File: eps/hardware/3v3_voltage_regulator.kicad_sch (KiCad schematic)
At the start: 16 parts, among them U39 MP28167-A

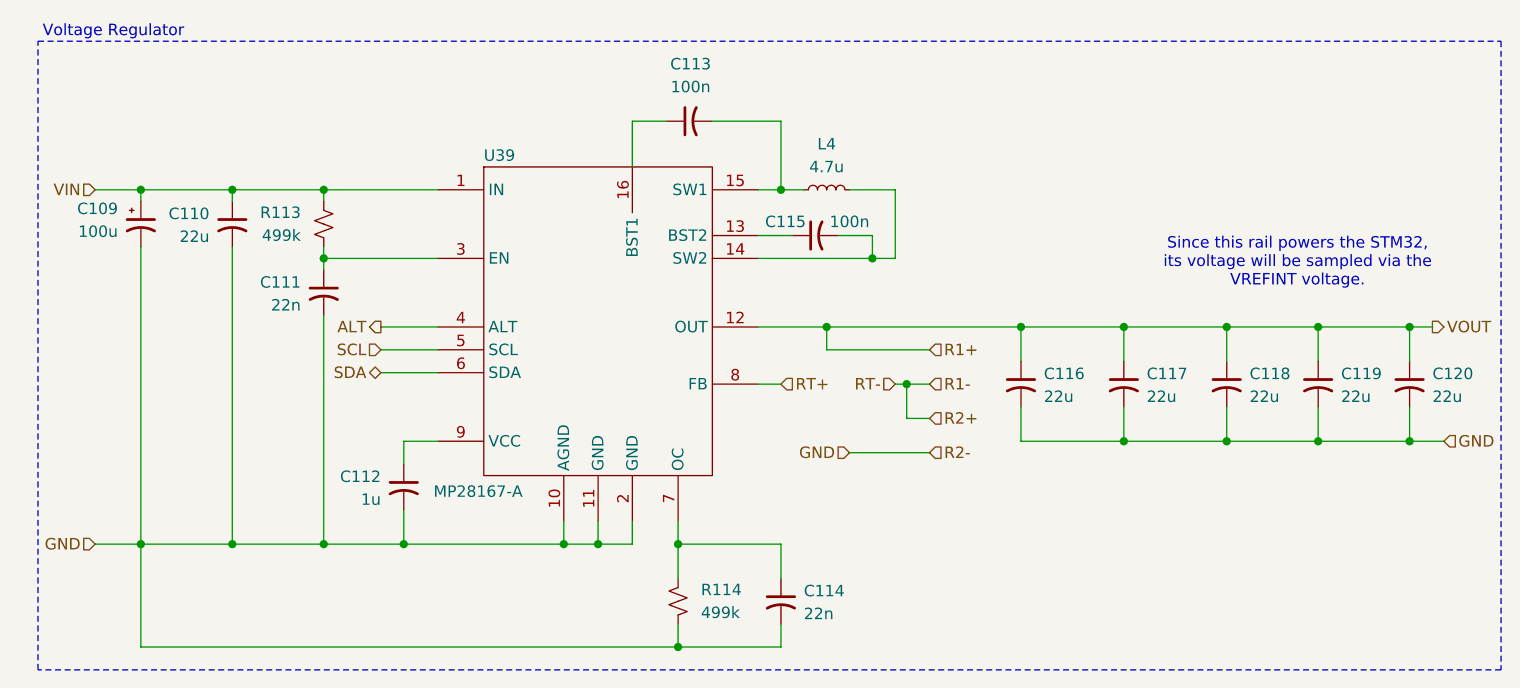
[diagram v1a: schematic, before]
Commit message: fix all ERC errors
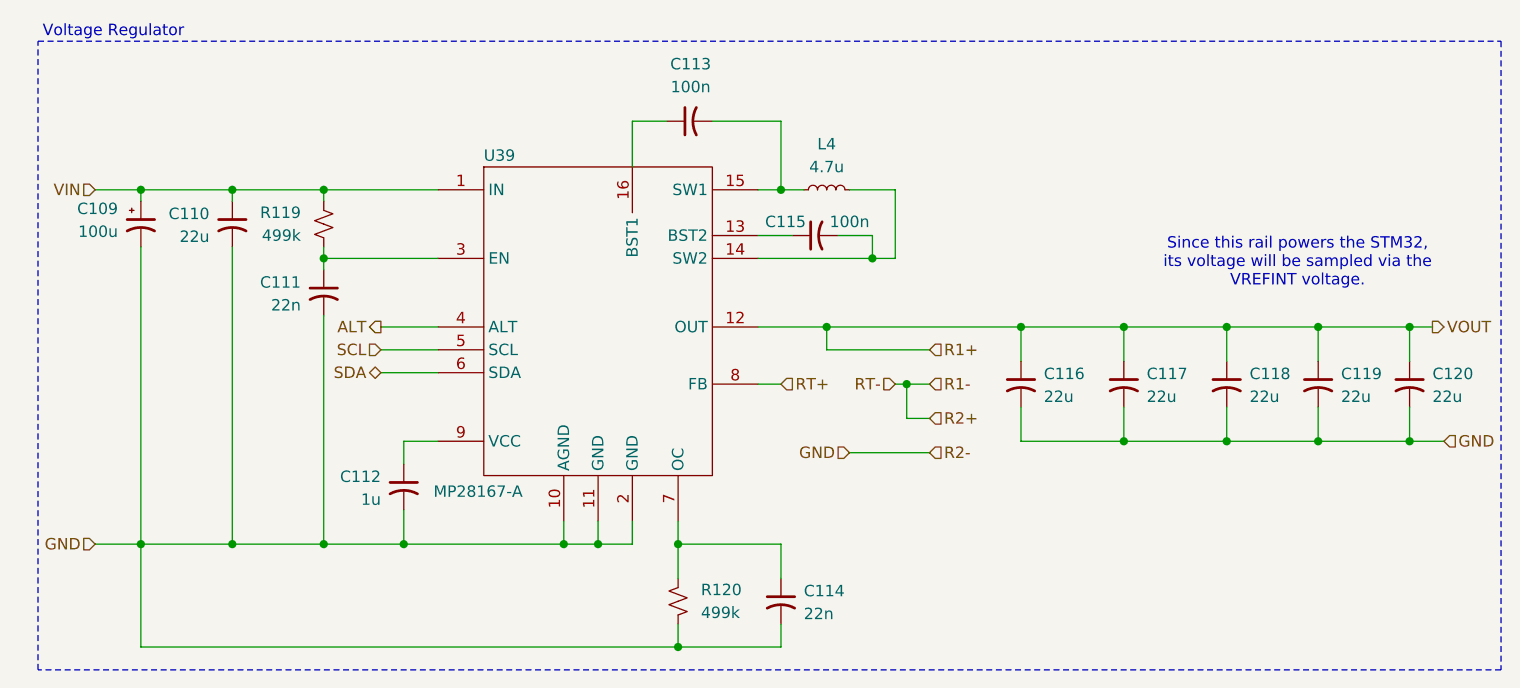
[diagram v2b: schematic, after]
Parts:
- renumbered R113 to R119, R114 to R120
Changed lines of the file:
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@@
 		(on_board yes)
 		(dnp no)
-		(property "Reference" "R113"
+		(property "Reference" "R119"
 			(at 107.95 78.7399 0)
 			(effects
@@
 			(project "eps"
 				(path "/9e0ae2e7-d4be-41b4-8312-0d2aceea2180/1a512821-4e0c-4fd8-8856-c70dc3f2d44d"
-					(reference "R113")
+					(reference "R119")
 					(unit 1)
 				)
@@
 		(on_board yes)
 		(dnp no)
-		(property "Reference" "R114"
+		(property "Reference" "R120"
 			(at 152.4 120.6499 0)
 			(effects
@@
 			(project "eps"
 				(path "/9e0ae2e7-d4be-41b4-8312-0d2aceea2180/1a512821-4e0c-4fd8-8856-c70dc3f2d44d"
-					(reference "R114")
+					(reference "R120")
 					(unit 1)
 				)

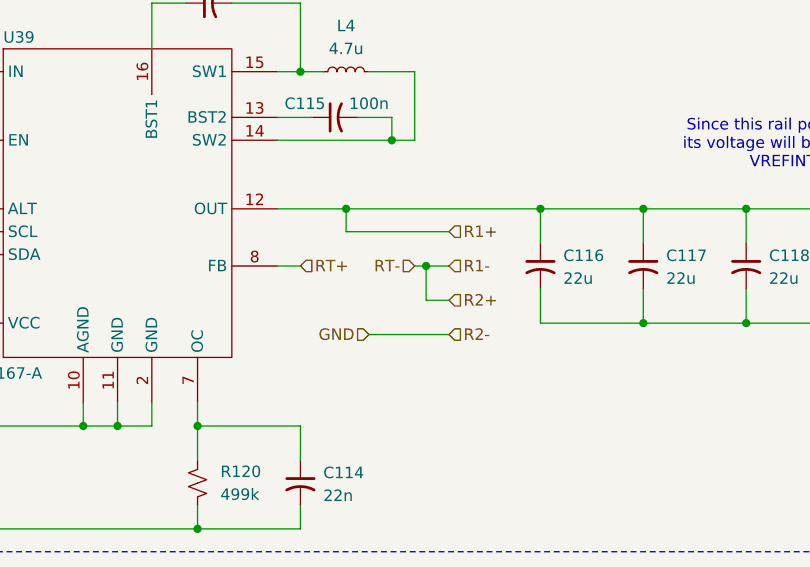
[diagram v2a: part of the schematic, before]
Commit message: fix all but one warning
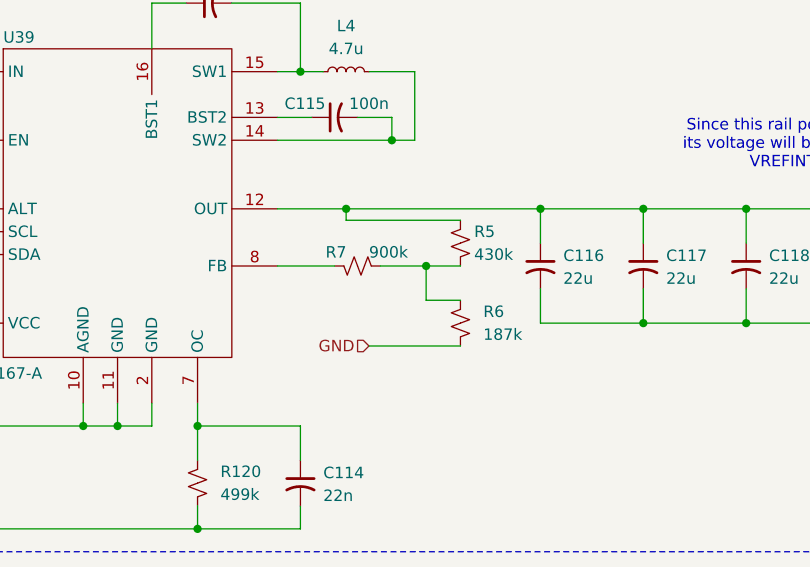
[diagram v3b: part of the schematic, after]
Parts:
- added R5: 430k, symbol Device:R_Small_US
- added R6: 187k, symbol Device:R_Small_US
- added R7: 900k, symbol Device:R_Small_US
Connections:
- net GND: now also R6.2
- net R1+ renamed VOUT
- net VOUT: now also R5.1
- net RT+: no longer names the net of U39.8 (FB)
- net RT+: now also R7.1
- new net: R5.2, R6.1, R7.2

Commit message: netlist fixes
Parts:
- renumbered R119 to R107, R120 to R108, R7 to R109, R5 to R110, R6 to R111
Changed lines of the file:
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@@
 		(on_board yes)
 		(dnp no)
-		(property "Reference" "R7"
-			(at 164.084 96.266 90)
+		(property "Reference" "R109"
+			(at 161.544 96.266 90)
 			(effects
 				(font
@@
 			(project "eps"
 				(path "/9e0ae2e7-d4be-41b4-8312-0d2aceea2180/1a512821-4e0c-4fd8-8856-c70dc3f2d44d"
-					(reference "R7")
+					(reference "R109")
 					(unit 1)
 				)
@@
 		(on_board yes)
 		(dnp no)
-		(property "Reference" "R5"
+		(property "Reference" "R110"
 			(at 180.594 93.98 0)
 			(effects
@@
 			(project "eps"
 				(path "/9e0ae2e7-d4be-41b4-8312-0d2aceea2180/1a512821-4e0c-4fd8-8856-c70dc3f2d44d"
-					(reference "R5")
+					(reference "R110")
 					(unit 1)
 				)
@@
 		(on_board yes)
 		(dnp no)
-		(property "Reference" "R6"
+		(property "Reference" "R111"
 			(at 181.61 102.8699 0)
 			(effects
@@
 			(project "eps"
 				(path "/9e0ae2e7-d4be-41b4-8312-0d2aceea2180/1a512821-4e0c-4fd8-8856-c70dc3f2d44d"
-					(reference "R6")
+					(reference "R111")
 					(unit 1)
 				)
@@
 		(on_board yes)
 		(dnp no)
-		(property "Reference" "R119"
+		(property "Reference" "R107"
 			(at 107.95 78.7399 0)
 			(effects
@@
 			(project "eps"
 				(path "/9e0ae2e7-d4be-41b4-8312-0d2aceea2180/1a512821-4e0c-4fd8-8856-c70dc3f2d44d"
-					(reference "R119")
+					(reference "R107")
 					(unit 1)
 				)
@@
 		(on_board yes)
 		(dnp no)
-		(property "Reference" "R120"
+		(property "Reference" "R108"
 			(at 152.4 120.6499 0)
 			(effects
@@
 			(project "eps"
 				(path "/9e0ae2e7-d4be-41b4-8312-0d2aceea2180/1a512821-4e0c-4fd8-8856-c70dc3f2d44d"
-					(reference "R120")
-					(unit 1)
-				)
+					(reference "R108")
+					(unit 1)
+				)

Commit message: start footprint assignment
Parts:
- C109: footprint (none) -> Capacitor_Tantalum_SMD:CP_EIA-3216-18_Kemet-A
- C110, C111, C112, C113, C114, C115, C116, C117, C118, C119, C120: footprint (none) -> Capacitor_SMD:C_0603_1608Metric
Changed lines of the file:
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@@
 			)
 		)
-		(property "Footprint" ""
+		(property "Footprint" "Capacitor_SMD:C_0603_1608Metric"
 			(at 220.98 97.79 0)
 			(effects
@@
 			)
 		)
-		(property "Footprint" ""
+		(property "Footprint" "Capacitor_SMD:C_0603_1608Metric"
 			(at 161.29 121.92 0)
 			(effects
@@
 			)
 		)
-		(property "Footprint" ""
+		(property "Footprint" "Capacitor_SMD:C_0603_1608Metric"
 			(at 119.38 109.22 0)
 			(effects
@@
 			)
 		)
-		(property "Footprint" ""
+		(property "Footprint" "Capacitor_SMD:C_0603_1608Metric"
 			(at 151.13 68.58 0)
 			(effects
@@
 			)
 		)
-		(property "Footprint" ""
+		(property "Footprint" "Capacitor_SMD:C_0603_1608Metric"
 			(at 231.14 97.79 0)
 			(effects
@@
 			)
 		)
-		(property "Footprint" ""
+		(property "Footprint" "Capacitor_SMD:C_0603_1608Metric"
 			(at 199.39 97.79 0)
 			(effects
@@
 			)
 		)
-		(property "Footprint" ""
+		(property "Footprint" "Capacitor_SMD:C_0603_1608Metric"
 			(at 187.96 97.79 0)
 			(effects
@@
 			)
 		)
-		(property "Footprint" ""
+		(property "Footprint" "Capacitor_SMD:C_0603_1608Metric"
 			(at 110.49 87.63 0)
 			(effects
@@
 			)
 		)
-		(property "Footprint" ""
+		(property "Footprint" "Capacitor_SMD:C_0603_1608Metric"
 			(at 100.33 80.01 0)
 			(effects
@@
 			)
 		)
-		(property "Footprint" ""
+		(property "Footprint" "Capacitor_SMD:C_0603_1608Metric"
 			(at 210.82 97.79 0)
 			(effects
@@
 			)
 		)
-		(property "Footprint" ""
+		(property "Footprint" "Capacitor_Tantalum_SMD:CP_EIA-3216-18_Kemet-A"
 			(at 90.17 80.01 0)
 			(effects
@@
 			)
 		)
-		(property "Footprint" ""
+		(property "Footprint" "Capacitor_SMD:C_0603_1608Metric"
 			(at 165.1 81.28 0)
 			(effects

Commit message: finish footprint assignment and board setup
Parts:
- L4: footprint (none) -> Inductor_SMD:L_Vishay_IHLP-2020
- R107, R108, R109, R110, R111: footprint (none) -> Resistor_SMD:R_0603_1608Metric
- U39: footprint (none) -> Package_DFN_QFN:MPS_QFN-16_3x3mm_P0.5mm
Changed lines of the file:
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@@
 			)
 		)
-		(property "Footprint" ""
+		(property "Footprint" "Package_DFN_QFN:MPS_QFN-16_3x3mm_P0.5mm"
 			(at 140.97 91.44 0)
 			(effects
@@
 			)
 		)
-		(property "Footprint" ""
+		(property "Footprint" "Resistor_SMD:R_0603_1608Metric"
 			(at 167.64 97.79 0)
 			(effects
@@
 			)
 		)
-		(property "Footprint" ""
+		(property "Footprint" "Inductor_SMD:L_Vishay_IHLP-2020"
 			(at 166.37 76.2 0)
 			(effects
@@
 			)
 		)
-		(property "Footprint" ""
+		(property "Footprint" "Resistor_SMD:R_0603_1608Metric"
 			(at 179.07 95.25 0)
 			(effects
@@
 			)
 		)
-		(property "Footprint" ""
+		(property "Footprint" "Resistor_SMD:R_0603_1608Metric"
 			(at 179.07 104.14 0)
 			(effects
@@
 			)
 		)
-		(property "Footprint" ""
+		(property "Footprint" "Resistor_SMD:R_0603_1608Metric"
 			(at 110.49 80.01 0)
 			(effects
@@
 			)
 		)
-		(property "Footprint" ""
+		(property "Footprint" "Resistor_SMD:R_0603_1608Metric"
 			(at 149.86 121.92 0)
 			(effects

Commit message: schematic fixes
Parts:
- C110, C111, C112, C113, C114, C115, C116, C117, C118, C119, C120: footprint Capacitor_SMD:C_0603_1608Metric -> Capacitor_SMD:C_0402_1005Metric
- R107, R108, R109, R110, R111: footprint Resistor_SMD:R_0603_1608Metric -> Resistor_SMD:R_0402_1005Metric
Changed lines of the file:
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@@
 			)
 		)
-		(property "Footprint" "Resistor_SMD:R_0603_1608Metric"
+		(property "Footprint" "Resistor_SMD:R_0402_1005Metric"
 			(at 167.64 97.79 0)
 			(effects
@@
 			)
 		)
-		(property "Footprint" "Capacitor_SMD:C_0603_1608Metric"
+		(property "Footprint" "Capacitor_SMD:C_0402_1005Metric"
 			(at 220.98 97.79 0)
 			(effects
@@
 			)
 		)
-		(property "Footprint" "Capacitor_SMD:C_0603_1608Metric"
+		(property "Footprint" "Capacitor_SMD:C_0402_1005Metric"
 			(at 161.29 121.92 0)
 			(effects
@@
 			)
 		)
-		(property "Footprint" "Capacitor_SMD:C_0603_1608Metric"
+		(property "Footprint" "Capacitor_SMD:C_0402_1005Metric"
 			(at 119.38 109.22 0)
 			(effects
@@
 			)
 		)
-		(property "Footprint" "Capacitor_SMD:C_0603_1608Metric"
+		(property "Footprint" "Capacitor_SMD:C_0402_1005Metric"
 			(at 151.13 68.58 0)
 			(effects
@@
 			)
 		)
-		(property "Footprint" "Capacitor_SMD:C_0603_1608Metric"
+		(property "Footprint" "Capacitor_SMD:C_0402_1005Metric"
 			(at 231.14 97.79 0)
 			(effects
@@
 			)
 		)
-		(property "Footprint" "Resistor_SMD:R_0603_1608Metric"
+		(property "Footprint" "Resistor_SMD:R_0402_1005Metric"
 			(at 179.07 95.25 0)
 			(effects
@@
 			)
 		)
-		(property "Footprint" "Capacitor_SMD:C_0603_1608Metric"
+		(property "Footprint" "Capacitor_SMD:C_0402_1005Metric"
 			(at 199.39 97.79 0)
 			(effects
@@
 			)
 		)
-		(property "Footprint" "Capacitor_SMD:C_0603_1608Metric"
+		(property "Footprint" "Capacitor_SMD:C_0402_1005Metric"
 			(at 187.96 97.79 0)
 			(effects
@@
 			)
 		)
-		(property "Footprint" "Capacitor_SMD:C_0603_1608Metric"
+		(property "Footprint" "Capacitor_SMD:C_0402_1005Metric"
 			(at 110.49 87.63 0)
 			(effects
@@
 			)
 		)
-		(property "Footprint" "Capacitor_SMD:C_0603_1608Metric"
+		(property "Footprint" "Capacitor_SMD:C_0402_1005Metric"
 			(at 100.33 80.01 0)
 			(effects
@@
 			)
 		)
-		(property "Footprint" "Resistor_SMD:R_0603_1608Metric"
+		(property "Footprint" "Resistor_SMD:R_0402_1005Metric"
 			(at 179.07 104.14 0)
 			(effects
@@
 			)
 		)
-		(property "Footprint" "Capacitor_SMD:C_0603_1608Metric"
+		(property "Footprint" "Capacitor_SMD:C_0402_1005Metric"
 			(at 210.82 97.79 0)
 			(effects
@@
 			)
 		)
-		(property "Footprint" "Resistor_SMD:R_0603_1608Metric"
+		(property "Footprint" "Resistor_SMD:R_0402_1005Metric"
 			(at 110.49 80.01 0)
 			(effects
@@
 			)
 		)
-		(property "Footprint" "Capacitor_SMD:C_0603_1608Metric"
+		(property "Footprint" "Capacitor_SMD:C_0402_1005Metric"
 			(at 165.1 81.28 0)
 			(effects
@@
 			)
 		)
-		(property "Footprint" "Resistor_SMD:R_0603_1608Metric"
+		(property "Footprint" "Resistor_SMD:R_0402_1005Metric"
 			(at 149.86 121.92 0)
 			(effects

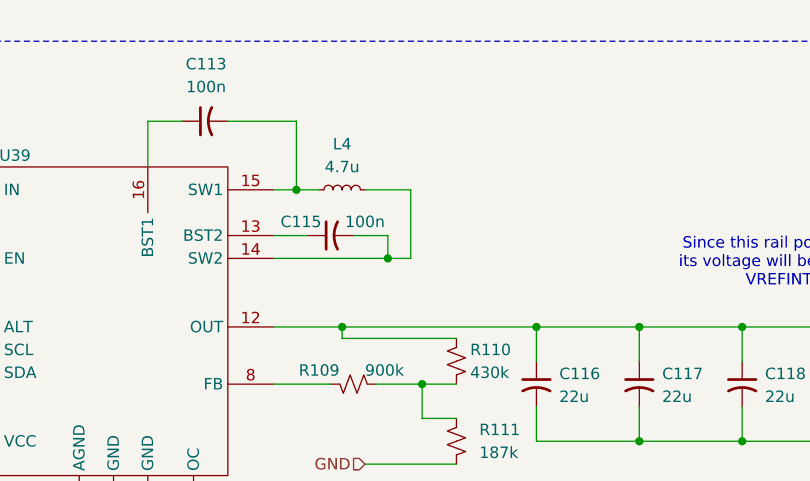
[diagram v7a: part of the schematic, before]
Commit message: fix placements and start routing voltage regulator
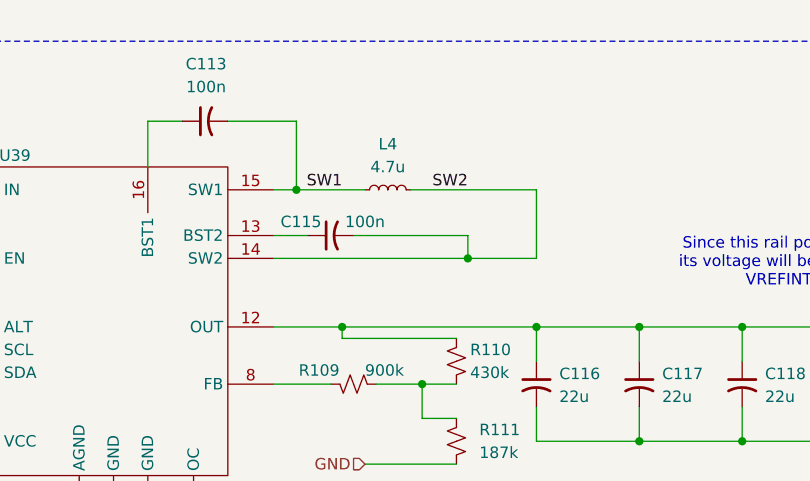
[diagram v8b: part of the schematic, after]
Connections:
- net SW2: now reaches C115.2, L4.2, U39.14 (SW2)
- net SW1: now reaches C113.2, L4.1, U39.15 (SW1)
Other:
- moved on the sheet: L4
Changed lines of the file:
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@@
-	)
-	(junction
-		(at 171.45 83.82)
-		(diameter 0)
-		(color 0 0 0 0)
 	)
 	(junction
@@
 	)
 	(junction
+		(at 137.16 115.57)
+		(diameter 0)
+		(color 0 0 0 0)
+	)
+	(junction
+		(at 210.82 91.44)
+		(diameter 0)
+		(color 0 0 0 0)
+	)
+	(junction
+		(at 149.86 115.57)
+		(diameter 0)
+		(color 0 0 0 0)
+	)
+	(junction
+		(at 166.37 91.44)
+		(diameter 0)
+		(color 0 0 0 0)
+	)
+	(junction
+		(at 119.38 115.57)
+		(diameter 0)
+		(color 0 0 0 0)
+	)
+	(junction
+		(at 231.14 91.44)
+		(diameter 0)
+		(color 0 0 0 0)
+	)
+	(junction
+		(at 110.49 83.82)
+		(diameter 0)
+		(color 0 0 0 0)
+	)
+	(junction
+		(at 140.97 115.57)
+		(diameter 0)
+		(color 0 0 0 0)
+	)
+	(junction
+		(at 110.49 76.2)
+		(diameter 0)
+		(color 0 0 0 0)
+	)
+	(junction
+		(at 220.98 91.44)
+		(diameter 0)
+		(color 0 0 0 0)
+	)
+	(junction
+		(at 187.96 91.44)
+		(diameter 0)
+		(color 0 0 0 0)
+	)
+	(junction
+		(at 90.17 115.57)
+		(diameter 0)
+		(color 0 0 0 0)
+	)
+	(junction
+		(at 210.82 104.14)
+		(diameter 0)
+		(color 0 0 0 0)
+	)
+	(junction
+		(at 90.17 76.2)
+		(diameter 0)
+		(color 0 0 0 0)
+	)
+	(junction
+		(at 175.26 97.79)
+		(diameter 0)
+		(color 0 0 0 0)
+	)
+	(junction
+		(at 199.39 104.14)
+		(diameter 0)
+		(color 0 0 0 0)
+	)
+	(junction
+		(at 110.49 115.57)
+		(diameter 0)
+		(color 0 0 0 0)
+	)
+	(junction
+		(at 100.33 115.57)
+		(diameter 0)
+		(color 0 0 0 0)
+	)
+	(junction
+		(at 180.34 83.82)
+		(diameter 0)
+		(color 0 0 0 0)
+	)
+	(junction
+		(at 231.14 104.14)
+		(diameter 0)
+		(color 0 0 0 0)
+	)
+	(junction
+		(at 100.33 76.2)
+		(diameter 0)
+		(color 0 0 0 0)
+	)
+	(junction
+		(at 220.98 104.14)
+		(diameter 0)
+		(color 0 0 0 0)
+	)
+	(junction
+		(at 199.39 91.44)
+		(diameter 0)
+		(color 0 0 0 0)
+	)
+	(junction
 		(at 161.29 76.2)
 		(diameter 0)
 		(color 0 0 0 0)
 	)
-	(junction
-		(at 137.16 115.57)
-		(diameter 0)
-		(color 0 0 0 0)
-	)
-	(junction
-		(at 210.82 91.44)
-		(diameter 0)
-		(color 0 0 0 0)
-	)
-	(junction
-		(at 149.86 115.57)
-		(diameter 0)
-		(color 0 0 0 0)
-	)
-	(junction
-		(at 166.37 91.44)
-		(diameter 0)
-		(color 0 0 0 0)
-	)
-	(junction
-		(at 119.38 115.57)
-		(diameter 0)
-		(color 0 0 0 0)
-	)
-	(junction
-		(at 231.14 91.44)
-		(diameter 0)
-		(color 0 0 0 0)
-	)
-	(junction
-		(at 110.49 83.82)
-		(diameter 0)
-		(color 0 0 0 0)
-	)
-	(junction
-		(at 140.97 115.57)
-		(diameter 0)
-		(color 0 0 0 0)
-	)
-	(junction
-		(at 110.49 76.2)
-		(diameter 0)
-		(color 0 0 0 0)
-	)
-	(junction
-		(at 220.98 91.44)
-		(diameter 0)
-		(color 0 0 0 0)
-	)
-	(junction
-		(at 187.96 91.44)
-		(diameter 0)
-		(color 0 0 0 0)
-	)
-	(junction
-		(at 90.17 115.57)
-		(diameter 0)
-		(color 0 0 0 0)
-	)
-	(junction
-		(at 210.82 104.14)
-		(diameter 0)
-		(color 0 0 0 0)
-	)
-	(junction
-		(at 90.17 76.2)
-		(diameter 0)
-		(color 0 0 0 0)
-	)
-	(junction
-		(at 175.26 97.79)
-		(diameter 0)
-		(color 0 0 0 0)
-	)
-	(junction
-		(at 199.39 104.14)
-		(diameter 0)
-		(color 0 0 0 0)
-	)
-	(junction
-		(at 110.49 115.57)
-		(diameter 0)
-		(color 0 0 0 0)
-	)
-	(junction
-		(at 100.33 115.57)
-		(diameter 0)
-		(color 0 0 0 0)
-	)
-	(junction
-		(at 231.14 104.14)
-		(diameter 0)
-		(color 0 0 0 0)
-	)
-	(junction
-		(at 100.33 76.2)
-		(diameter 0)
-		(color 0 0 0 0)
-	)
-	(junction
-		(at 220.98 104.14)
-		(diameter 0)
-		(color 0 0 0 0)
-	)
-	(junction
-		(at 199.39 91.44)
-		(diameter 0)
-		(color 0 0 0 0)
-	)
 	(wire
 		(pts
@@
 	(wire
 		(pts
-			(xy 167.64 81.28) (xy 171.45 81.28)
+			(xy 161.29 76.2) (xy 168.91 76.2)
+		)
+		(stroke
+			(width 0)
+			(type default)
+		)
+	)
+	(wire
+		(pts
+			(xy 167.64 81.28) (xy 180.34 81.28)
 		)
 		(stroke
@@
 	(wire
 		(pts
-			(xy 158.75 76.2) (xy 161.29 76.2)
-		)
-		(stroke
-			(width 0)
-			(type default)
-		)
-	)
-	(wire
-		(pts
 			(xy 220.98 100.33) (xy 220.98 104.14)
 		)
@@
 	(wire
 		(pts
+			(xy 161.29 76.2) (xy 158.75 76.2)
+		)
+		(stroke
+			(width 0)
+			(type default)
+		)
+	)
+	(wire
+		(pts
 			(xy 231.14 104.14) (xy 234.95 104.14)
 		)
@@
 	(wire
 		(pts
-			(xy 158.75 83.82) (xy 171.45 83.82)
+			(xy 158.75 83.82) (xy 180.34 83.82)
 		)
 		(stroke
@@
 	(wire
 		(pts
-			(xy 171.45 81.28) (xy 171.45 83.82)
+			(xy 180.34 81.28) (xy 180.34 83.82)
 		)
 		(stroke
@@
 	(wire
 		(pts
-			(xy 173.99 76.2) (xy 173.99 83.82)
+			(xy 187.96 76.2) (xy 187.96 83.82)
 		)
 		(stroke
@@
 	(wire
 		(pts
-			(xy 161.29 76.2) (xy 163.83 76.2)
-		)
-		(stroke
-			(width 0)
-			(type default)
-		)
-	)
-	(wire
-		(pts
 			(xy 220.98 91.44) (xy 231.14 91.44)
 		)
@@
 	(wire
 		(pts
-			(xy 173.99 83.82) (xy 171.45 83.82)
+			(xy 187.96 83.82) (xy 180.34 83.82)
 		)
 		(stroke
@@
 	(wire
 		(pts
-			(xy 168.91 76.2) (xy 173.99 76.2)
+			(xy 173.99 76.2) (xy 187.96 76.2)
 		)
 		(stroke
@@
 			(width 0)
 			(type default)
+		)
+	)
+	(label "SW2"
+		(at 180.34 76.2 180)
+		(effects
+			(font
+				(size 1.27 1.27)
+			)
+			(justify right bottom)
+		)
+	)
+	(label "SW1"
+		(at 166.37 76.2 180)
+		(effects
+			(font
+				(size 1.27 1.27)
+			)
+			(justify right bottom)
 		)
 	)
@@
 	(symbol
 		(lib_id "Device:L_Small")
-		(at 166.37 76.2 90)
+		(at 171.45 76.2 90)
 		(unit 1)
 		(exclude_from_sim no)
@@
 		(fields_autoplaced yes)
 		(property "Reference" "L4"
-			(at 166.37 71.12 90)
+			(at 171.45 71.12 90)
 			(effects
 				(font
@@
 		)
 		(property "Value" "4.7u"
-			(at 166.37 73.66 90)
+			(at 171.45 73.66 90)
 			(effects
 				(font
@@
 		)
 		(property "Footprint" "Inductor_SMD:L_Vishay_IHLP-2020"
-			(at 166.37 76.2 0)
+			(at 171.45 76.2 0)
 			(effects
 				(font
@@
 		)
 		(property "Datasheet" "~"
-			(at 166.37 76.2 0)
+			(at 171.45 76.2 0)
 			(effects
 				(font
@@
 		)
 		(property "Description" "Inductor, small symbol"
-			(at 166.37 76.2 0)
-			(effects
-				(font
+			(at 171.45 76.2 0)
+			(effects
+				(font
